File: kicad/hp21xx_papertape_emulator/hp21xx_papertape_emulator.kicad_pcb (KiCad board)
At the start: 2 copper layers, 62.5 x 61.1 mm, 79 parts, among them J1 SWD, J2 SERIAL, J3 Micro_SD_Card_Det_Hirose_DM3AT, J4 HP Microcircuit, SW1 Select, SW2 Up, SW3 Down, U1 TLV75533PDRV, U2 STM32F103C8Tx, U3 USBLC6-2SC6, U4 74AHC1GU04, U5 74HCT245, U6 74LVC1G04, U7 74LVC245, Y1 8MHz

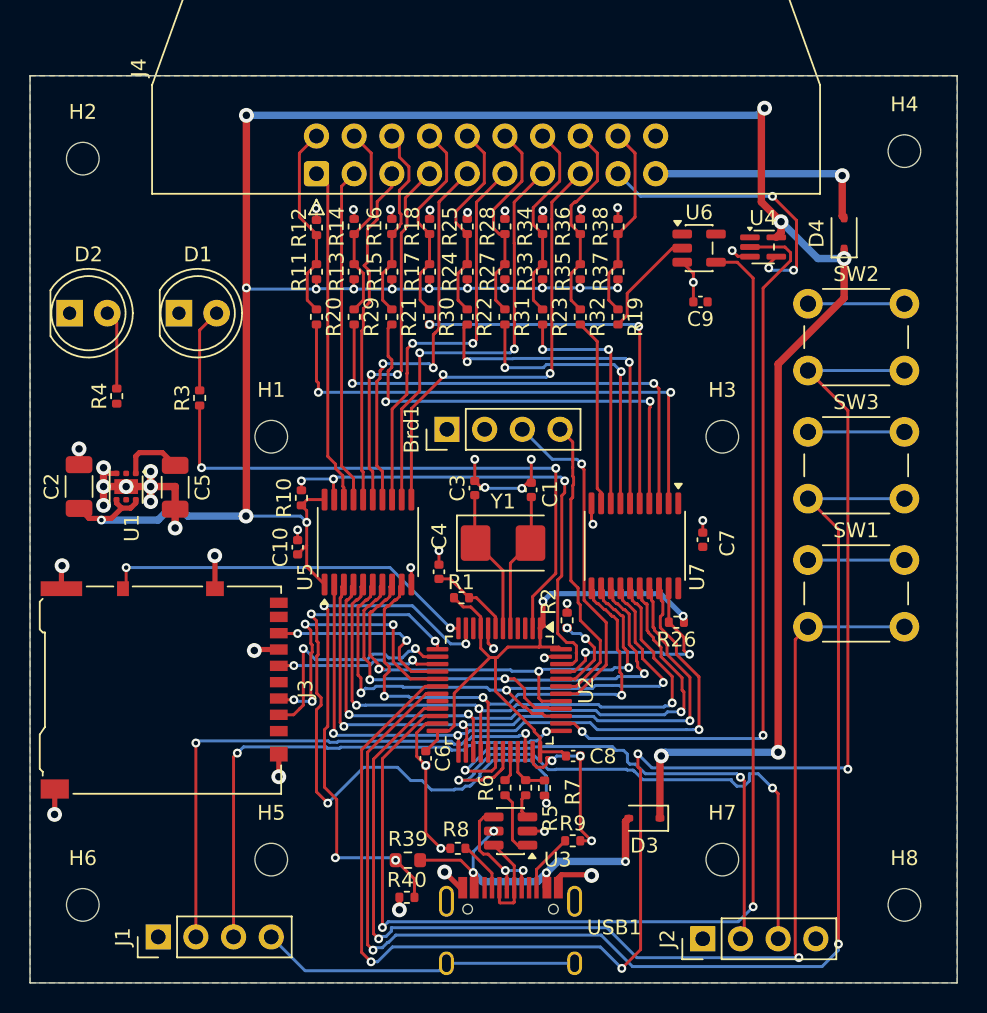
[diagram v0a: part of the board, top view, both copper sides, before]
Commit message: Almost done. Waiting for confirming OLED display and buttons dimensions.
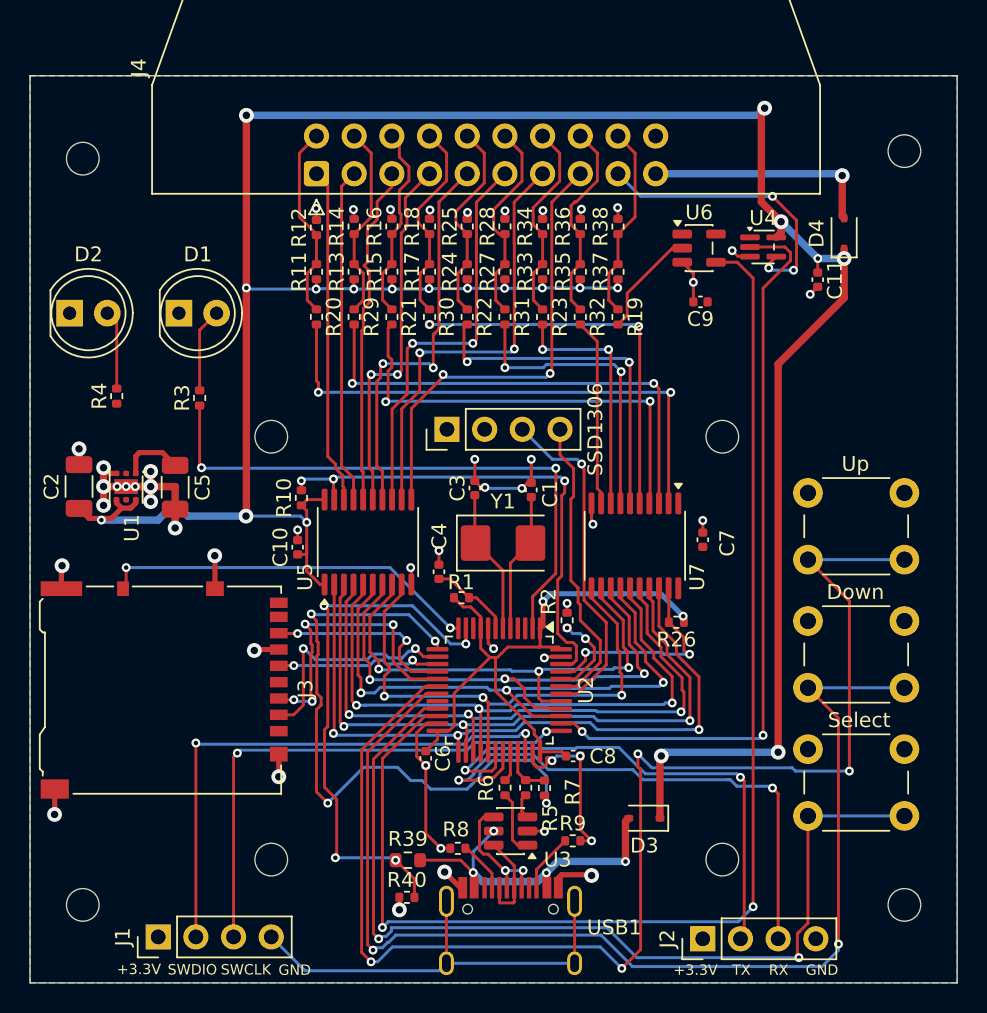
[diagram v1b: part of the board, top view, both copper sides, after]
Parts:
- added C11: 100n, Capacitor_SMD:C_0402_1005Metric, F.Cu at (103.4, 56.4)
- R12, R14, R16, R18, R25, R28, R34, R36, R38: value 820 -> 1k
- moved SW2 12.7 mm to (102.7, 70.8)
- moved SW3 12.7 mm to (102.7, 79.4)
- moved SW1 12.7 mm to (102.7, 88.1)
- renumbered Brd1 to OLED1
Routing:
- net Net-(U2-PB10): track 76.8 -> 64.0 mm
- net Net-(U2-PB1): track 90.7 -> 78.0 mm
- net Net-(U2-PB0): track 103.5 -> 91.0 mm
- net GND: track 119.4 -> 108.9 mm, vias 46 -> 49
- net +5V: track 184.0 -> 185.4 mm, vias 19 -> 20
- net Net-(J2-Pin_3): track 38.7 -> 37.7 mm
- net /D6: track 33.8 -> 33.1 mm
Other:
- board text added: "+3.3V"
- board text added: "+5V"
- board text added: "CMD"
- board text added: "FLAG"
- board text added: "GND"
- board text added: "HP 21XX Paper Tape Emulator"
- board text added: "IN0"
- board text added: "IN1"
- board text added: "IN2"
- board text added: "IN3"
- board text added: "IN4"
- board text added: "IN5"
- board text added: "IN6"
- board text added: "IN7"
- board text added: "Mattis Lind 2026"
- board text added: "OUT0"
- board text added: "OUT1"
- board text added: "OUT2"
- board text added: "OUT3"
- board text added: "OUT4"
- board text added: "OUT5"
- board text added: "OUT6"
- board text added: "OUT7"
- board text added: "RX"
- board text added: "SWCLK"
- board text added: "SWDIO"
- board text added: "TX"
- board text added: "https://github.com/MattisLind/hp21xx_papertape_emulator"
- board text added: "www.datormuseum.se"

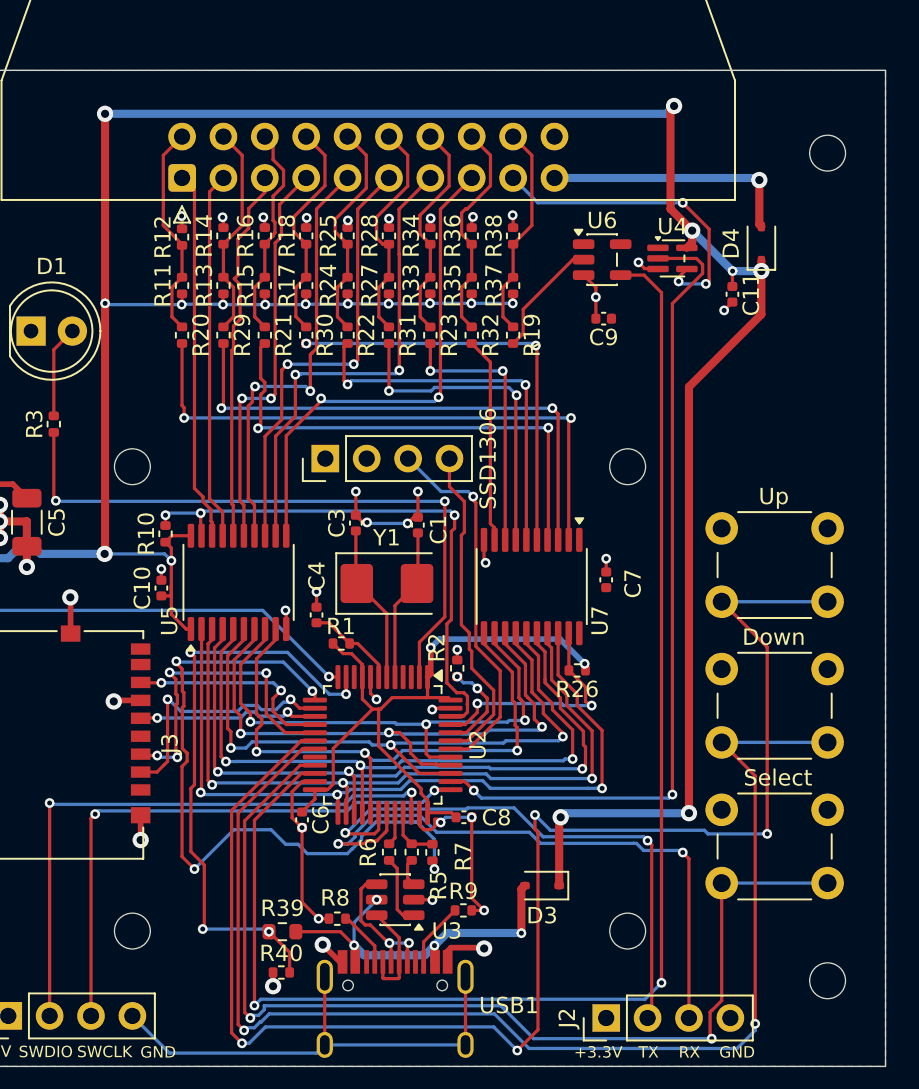
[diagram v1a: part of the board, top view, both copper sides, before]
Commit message: Added paper out handling.
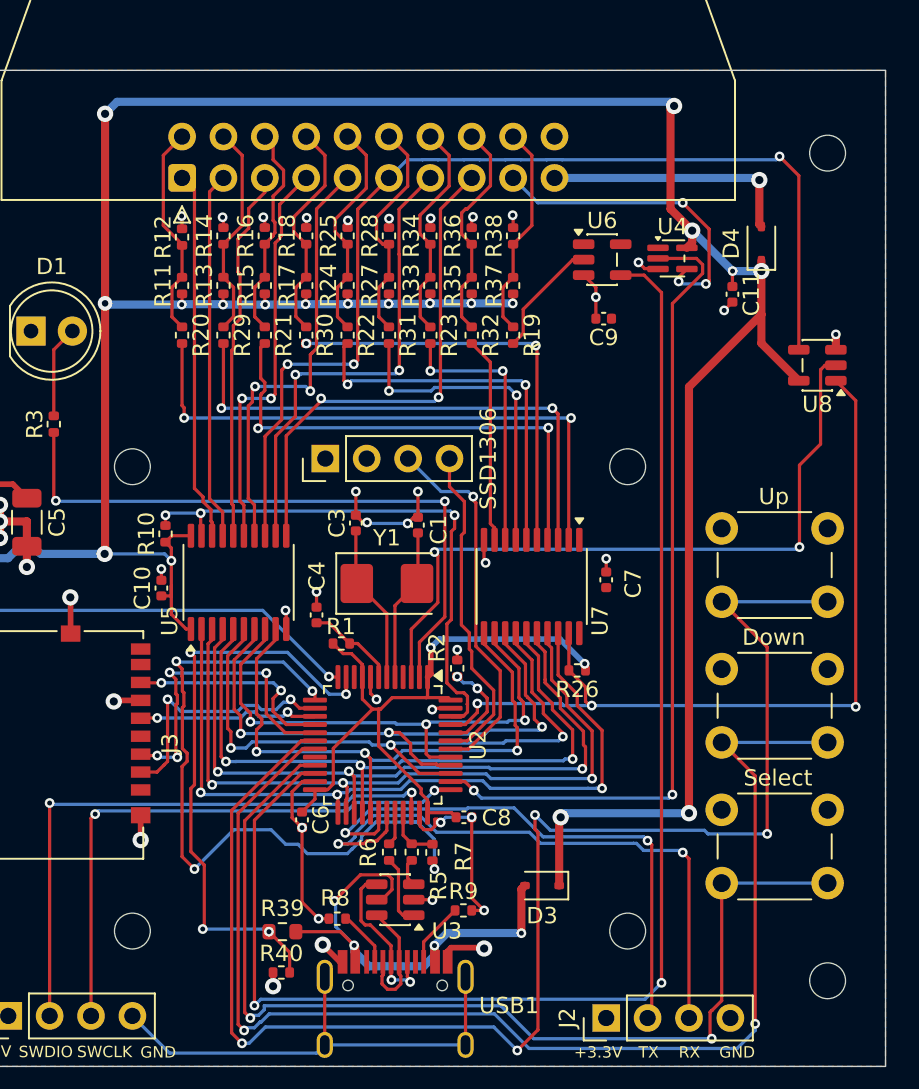
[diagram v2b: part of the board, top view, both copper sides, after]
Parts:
- added U8: 74AHCT1G125, Package_TO_SOT_SMD:SOT-23-5, F.Cu at (108.6, 60.8)
- U4: value 74AHC1GU04 -> 74AHCT1G04SE-7
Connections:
- U2 pad 3: unconnected-(U2-PC14-Pad3) -> /PAPEROUT
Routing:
- net /PAPEROUT: track 0.00 -> 43.4 mm, vias 0 -> 2
- net Net-(J4-Pin_11): track 27.5 -> 64.4 mm, vias 2 -> 3
- net /PUNEN: track 14.7 -> 51.4 mm, vias 2 -> 3
- net Net-(D3-A): track 23.5 -> 30.6 mm
- net +5V: track 185.4 -> 190.7 mm
- net Net-(USB1-DP1): track 9.05 -> 10.3 mm
- net Net-(USB1-DN1): track 6.43 -> 7.64 mm
- net GND: track 108.9 -> 109.9 mm, vias 49 -> 50

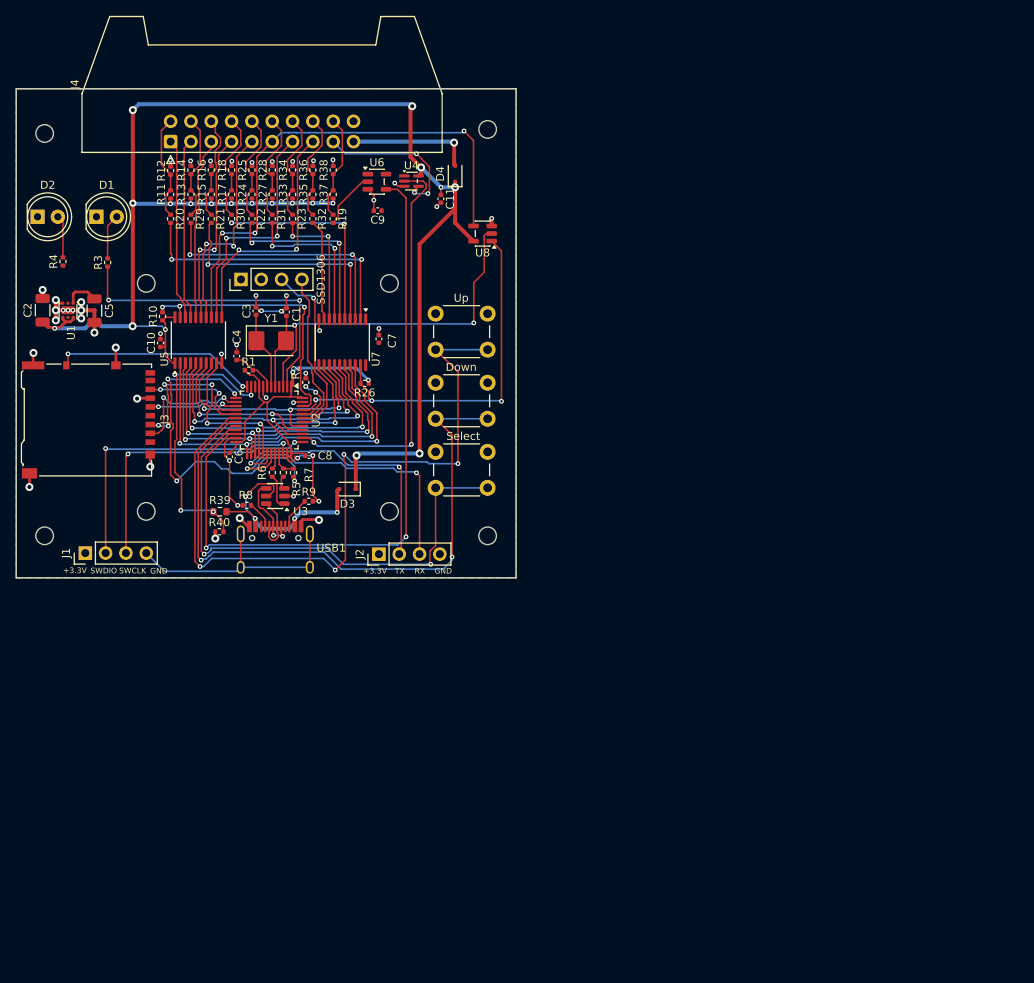
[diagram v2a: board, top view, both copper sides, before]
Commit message: Updates to support simultaneous PTR and PTP. Able yo use 540 and 541 instead of 245 if not available.
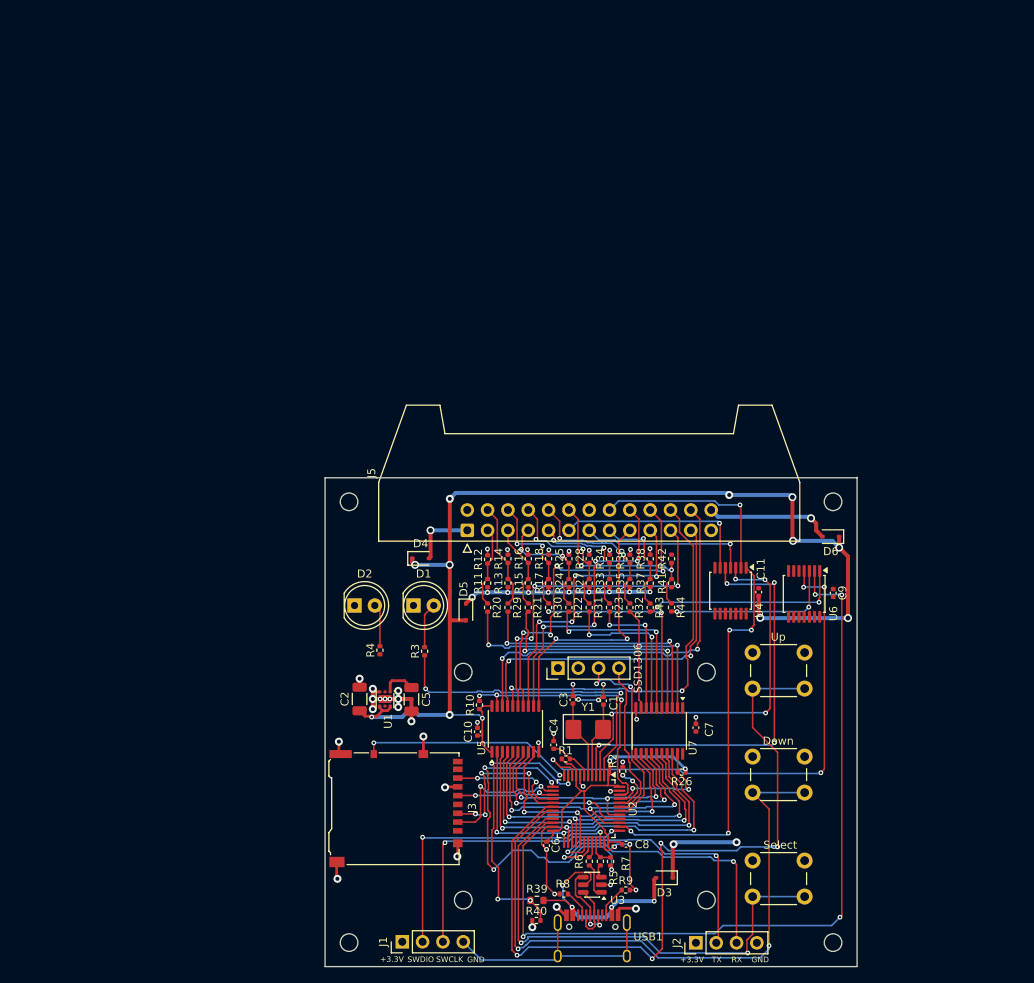
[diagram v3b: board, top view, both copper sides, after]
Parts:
- removed J4: HP Microcircuit, Connector_IDC:IDC-Header_2x10_P2.54mm_Latch_Horizontal
- removed R19: 220, Resistor_SMD:R_0402_1005Metric
- removed U8: 74AHCT1G125, Package_TO_SOT_SMD:SOT-23-5
- added D5: 1N5819WS, Diode_SMD:D_SOD-323, F.Cu at (106.5, 108.1)
- added D6: 1N5819WS, Diode_SMD:D_SOD-323, F.Cu at (152.1, 98.7)
- added J5: Conn_02x13_Odd_Even, Connector_IDC:IDC-Header_2x13_P2.54mm_Latch_Horizontal, F.Cu at (106.7, 97.9)
- added R41: 330, Resistor_SMD:R_0402_1005Metric, F.Cu at (132.2, 104.5)
- added R42: 1k, Resistor_SMD:R_0402_1005Metric, F.Cu at (132.2, 101.4)
- added R43: 220, Resistor_SMD:R_0402_1005Metric, F.Cu at (129.5, 107.5)
- added R44: 220, Resistor_SMD:R_0402_1005Metric, F.Cu at (132.2, 107.5)
- U4: value 74AHCT1G04SE-7 -> 74HCT04; footprint Package_TO_SOT_SMD:SOT-353_SC-70-5 -> Package_SO:TSSOP-14_4.4x5mm_P0.65mm
- U6: value 74LVC1G04 -> 74LVC14; footprint Package_TO_SOT_SMD:SOT-23-5 -> Package_SO:TSSOP-14_4.4x5mm_P0.65mm
- moved C9 74.3 mm to (152.4, 105.7), turned to -90 degrees
- moved U6 74.2 mm to (148.8, 105.8), turned to -90 degrees
- moved H8 66.7 mm to (152.4, 149.4)
- moved U4 64.9 mm to (139.6, 105.4), turned to -90 degrees
- moved SW1 64.7 mm to (142.3, 139.2)
- moved H6 63.5 mm to (91.9, 149.4)
- moved H4 63.5 mm to (152.4, 94.3)
- moved C11 63.2 mm to (143.1, 105.6), turned to 90 degrees
- moved C3 62.7 mm to (119.9, 119.0)
- moved H7 62.7 mm to (136.6, 144.1)
- moved U3 62.7 mm to (122.3, 142.2)
- moved USB1 62.7 mm to (122.3, 153.7)
- moved C10 62.7 mm to (108.0, 123.0)
- moved D3 62.7 mm to (131.3, 141.3)
- moved H3 62.7 mm to (136.6, 115.6)
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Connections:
- net /INC renamed /INCR
- R11 pad 1: +5V -> Net-(D5-K)
- R13 pad 1: +5V -> Net-(D5-K)
- R15 pad 1: +5V -> Net-(D5-K)
- R17 pad 1: +5V -> Net-(D5-K)
- R24 pad 1: +5V -> Net-(D5-K)
- R27 pad 1: +5V -> Net-(D5-K)
- R33 pad 1: +5V -> Net-(D5-K)
- R35 pad 1: +5V -> Net-(D5-K)
- R37 pad 1: +5V -> Net-(D5-K)
- U2 pad 10: unconnected-(U2-PA0-Pad10) -> /CMD_PTP
- U2 pad 22: /CMD -> /CMD_PTR
- U2 pad 38: /FLAG -> /FLAG_PTR
- U2 pad 4: unconnected-(U2-PC15-Pad4) -> /FLAG_PTP
- U4 pad 1: unconnected-(U4-NC-Pad1) -> /FLAG_PTR
- U4 pad 2: /FLAG -> /OUTFR
- U4 pad 3: GND -> /PAPEROUT
- U4 pad 4: Net-(J4-Pin_17) -> /PAPER_LOW
- U4 pad 5: +5V -> /FLAG_PTP
- U5 pad 11: Net-(J4-Pin_15) -> /OUT7
- U5 pad 12: Net-(J4-Pin_13) -> /OUT6
- U5 pad 13: Net-(J4-Pin_11) -> /OUT5
- U5 pad 14: Net-(J4-Pin_9) -> /OUT4
- U5 pad 15: Net-(J4-Pin_7) -> /OUT3
- U5 pad 16: Net-(J4-Pin_5) -> /OUT2
- U5 pad 17: Net-(J4-Pin_3) -> /OUT1
- U5 pad 18: Net-(J4-Pin_1) -> /OUT0
- U6 pad 1: unconnected-(U6-NC-Pad1) -> Net-(R43-Pad2)
- U6 pad 2: Net-(R19-Pad2) -> /CMD_PTR
- U6 pad 3: GND -> Net-(R44-Pad2)
- U6 pad 4: /CMD -> /CMD_PTP
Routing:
- net /CMD_PTR: track 0.00 -> 103.6 mm, vias 0 -> 4
- net /CMD: track 87.2 -> 0.00 mm, vias 2 -> 0
- net /CMD_PTP: track 0.00 -> 65.9 mm, vias 0 -> 4
- net Net-(J4-Pin_11): track 64.4 -> 0.00 mm, vias 3 -> 0
- net /FLAG_PTP: track 0.00 -> 54.1 mm, vias 0 -> 4
- net /FLAG_PTR: track 0.00 -> 50.6 mm, vias 0 -> 4
- net /FLAG: track 50.3 -> 0.00 mm, vias 2 -> 0
- net /OUT0: track 0.00 -> 49.6 mm, vias 0 -> 2
- net /OUT2: track 0.00 -> 48.5 mm, vias 0 -> 2
- net /OUT1: track 0.00 -> 45.2 mm, vias 0 -> 2
- net /OUT4: track 0.00 -> 44.0 mm, vias 0 -> 4
- net /OUT3: track 0.00 -> 42.3 mm, vias 0 -> 4
- net /OUT5: track 0.00 -> 37.4 mm, vias 0 -> 4
- net /OUT6: track 0.00 -> 37.1 mm, vias 0 -> 4
- net /PUNEN: track 51.4 -> 14.7 mm, vias 3 -> 2
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- removed copper zone on F.Cu, net +3.3V
- removed copper zone on B.Cu, net GND
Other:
- board size 62.5 x 61.1 mm -> 66.5 x 61.2 mm
